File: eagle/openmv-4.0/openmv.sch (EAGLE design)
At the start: 52 parts, among them U1 OV9650, U2 USD-47571, U3 ADP222, U4 STM32F407LQFP100, U5 BEAD, U6 BEAD, U7 24FC128, X1 USB-MICROB, Y2 RESONATORSMD

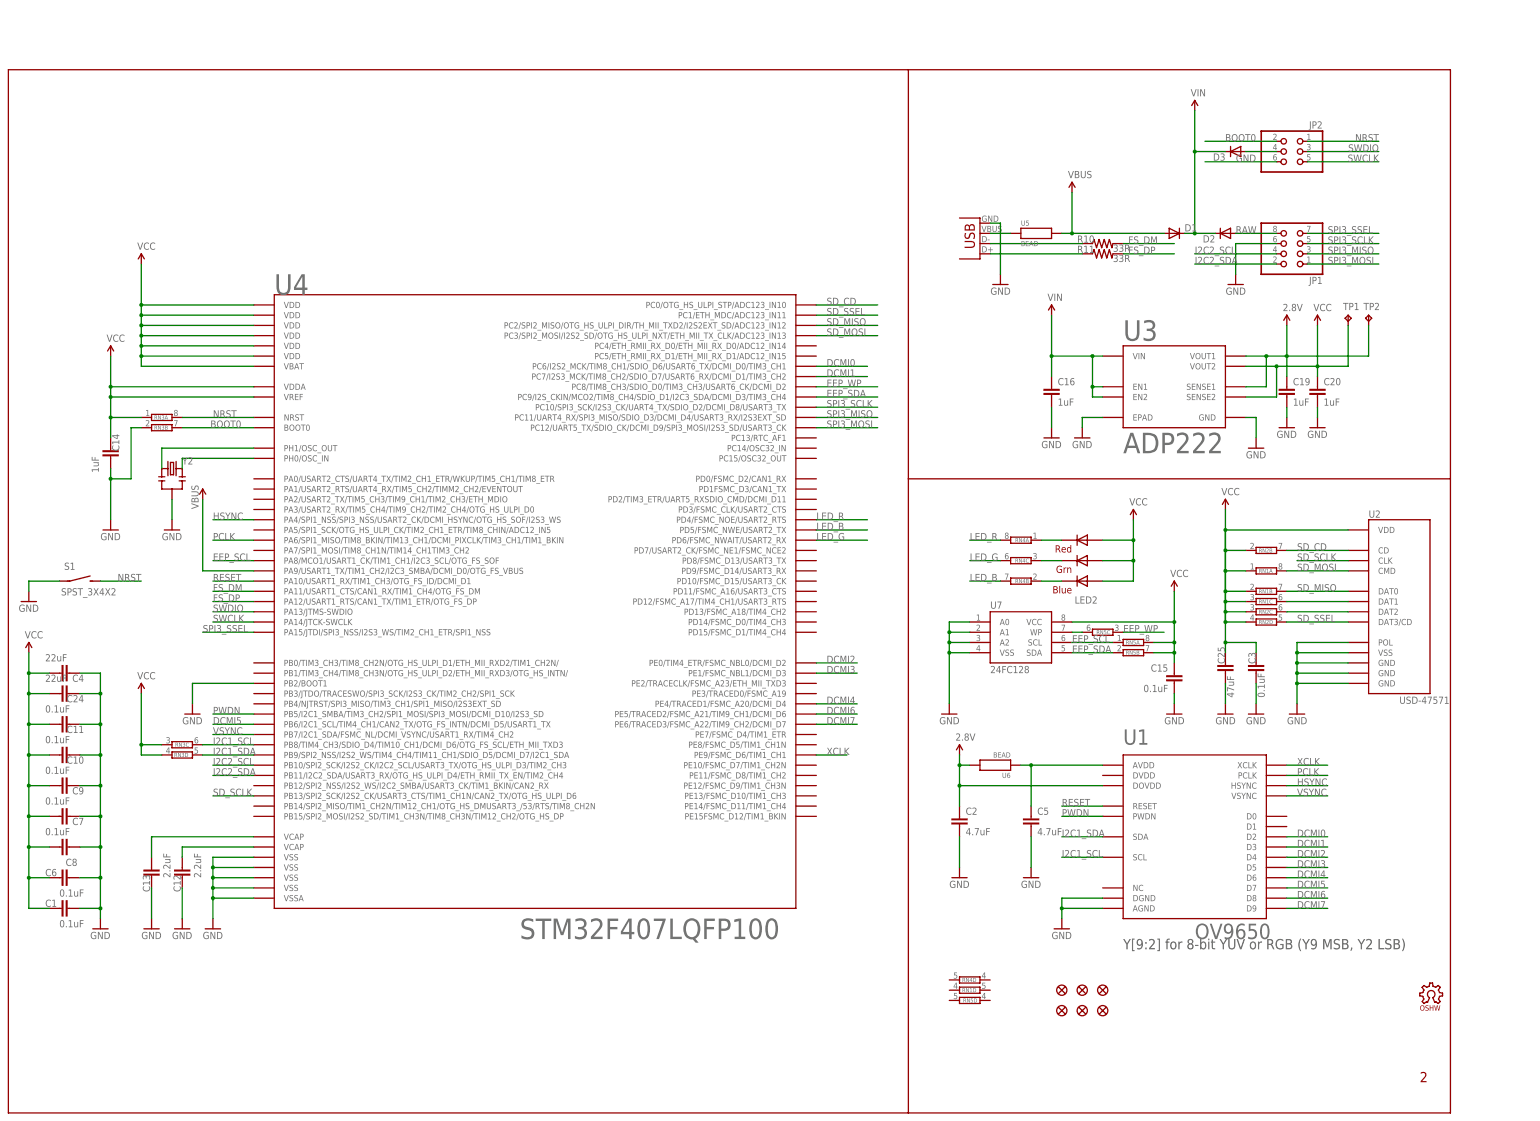
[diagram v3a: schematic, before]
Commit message: Update REV4
* Make more room for mounting holes, and dbg header
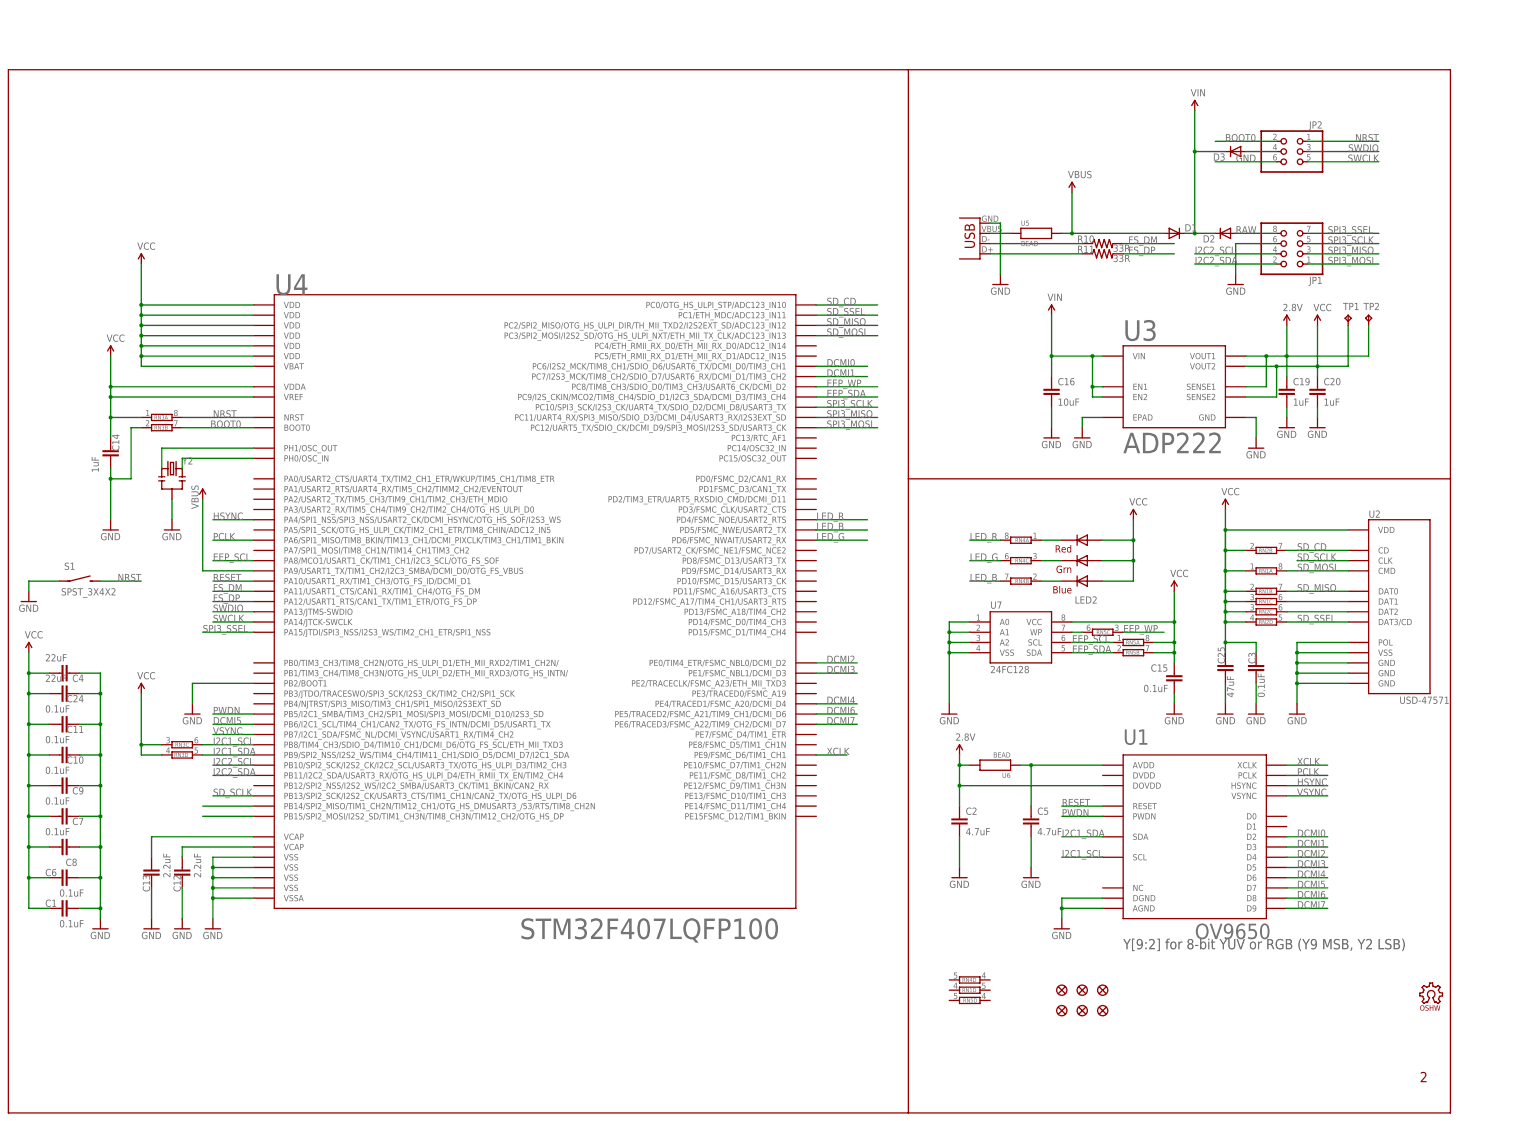
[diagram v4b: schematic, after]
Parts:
- C16: value 1uF -> 10uF; device sfe:CAP0402-CAP -> sfe:CAP0805
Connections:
- new net N$12: U4.PB14/SPI2_MISO/TIM1_CH2N/TIM12_CH1/OTG_HS_DMUSART3_/53/RTS/TIM8_CH2N
- new net N$13: U4.PB15/SPI2_MOSI/I2S2_SD/TIM1_CH3N/TIM8_CH3N/TIM12_CH2/OTG_HS_DP
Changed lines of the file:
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@@
 <part name="U$6" library="mux" deviceset="VBUS" device=""/>
 <part name="LOGO1" library="iofault" deviceset="OSHW_LOGO_FILL" device="X0150-NT"/>
-<part name="C16" library="sfe" deviceset="CAP" device="0402-CAP" value="1uF"/>
+<part name="C16" library="sfe" deviceset="CAP" device="0805" value="10uF"/>
 <part name="GND11" library="SparkFun" deviceset="GND" device=""/>
 <part name="C20" library="sfe" deviceset="CAP" device="0402-CAP" value="1uF"/>
@@
 <segment>
 <pinref part="JP2" gate="A" pin="6"/>
-<wire x1="205.74" y1="134.62" x2="187.96" y2="134.62" width="0.1524" layer="91"/>
+<wire x1="205.74" y1="134.62" x2="190.5" y2="134.62" width="0.1524" layer="91"/>
 <label x="200.66" y="134.62" size="1.778" layer="95" rot="MR0"/>
 </segment>
@@
 <segment>
 <pinref part="JP2" gate="A" pin="2"/>
-<wire x1="205.74" y1="139.7" x2="187.96" y2="139.7" width="0.1524" layer="91"/>
+<wire x1="205.74" y1="139.7" x2="190.5" y2="139.7" width="0.1524" layer="91"/>
 <label x="200.66" y="139.7" size="1.778" layer="95" rot="MR0"/>
 </segment>
@@
 </segment>
 </net>
+<net name="N$12" class="0">
+<segment>
+<pinref part="U4" gate="G$1" pin="PB14/SPI2_MISO/TIM1_CH2N/TIM12_CH1/OTG_HS_DMUSART3_/53/RTS/TIM8_CH2N"/>
+<wire x1="-48.26" y1="-25.4" x2="-60.96" y2="-25.4" width="0.1524" layer="91"/>
+</segment>
+</net>
+<net name="N$13" class="0">
+<segment>
+<pinref part="U4" gate="G$1" pin="PB15/SPI2_MOSI/I2S2_SD/TIM1_CH3N/TIM8_CH3N/TIM12_CH2/OTG_HS_DP"/>
+<wire x1="-48.26" y1="-27.94" x2="-60.96" y2="-27.94" width="0.1524" layer="91"/>
+</segment>
+</net>

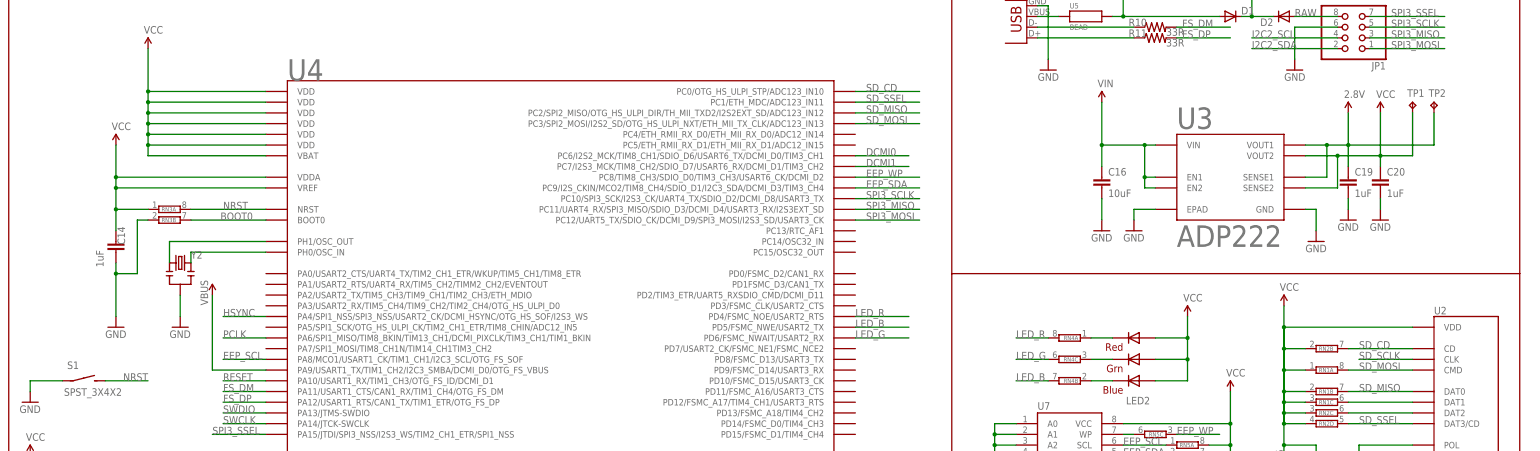
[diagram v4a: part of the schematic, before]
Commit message: Update REV4
* Replace regulator with ADP121xx
* Use the new crystal
* Fix USB connector
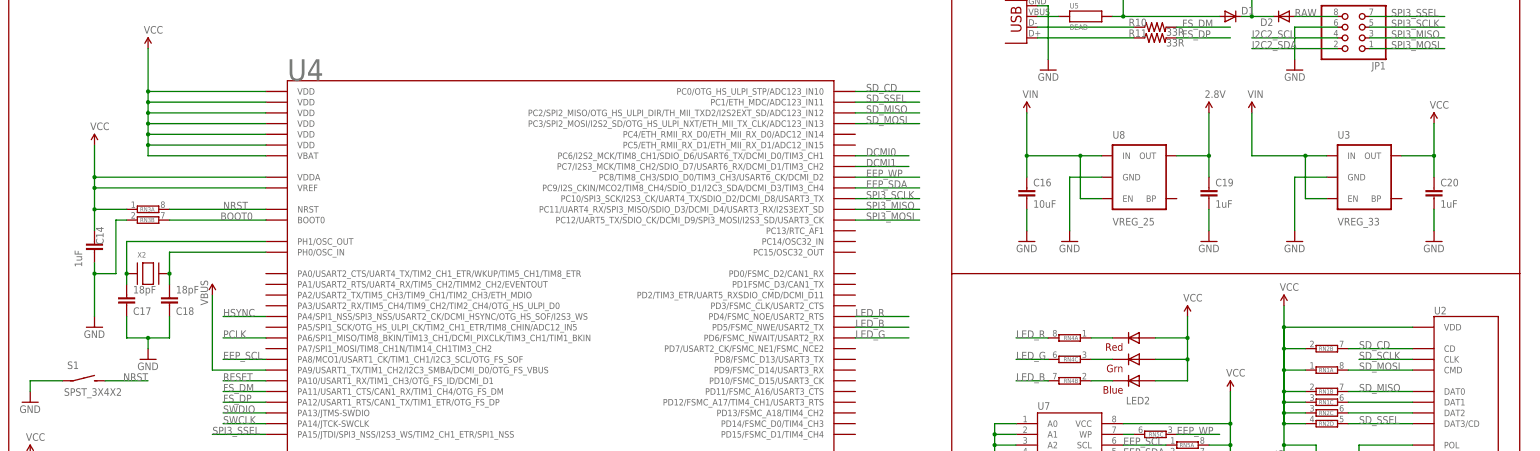
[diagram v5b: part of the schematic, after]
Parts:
- removed TP1, TP2: TPTP10R, testpad:TPTP10R
- removed Y2: RESONATORSMD, sfe:RESONATORSMD
- added C17, C18: 18pF, sfe:CAP0402-CAP
- added U8: VREG_25, sfe:V_REG_LDOSMD
- added X2: (no value), adafruit:XTALNX5032
- U3: value ADP222 -> VREG_33; device mux:ADP222 -> sfe:V_REG_LDOSMD
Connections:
- net 2.8V: now also U8.OUT; no longer TP2.TP, U3.SENSE1, U3.VOUT1
- net GND: now also C17.1, C18.1, U8.GND; no longer U3.EPAD, Y2.2
- net N$6: now also C17.2, X2.P$1; no longer Y2.1
- net N$8: now also C18.2, X2.P$2; no longer Y2.3
- net VCC: now also U3.OUT; no longer TP1.TP, U3.SENSE2, U3.VOUT2
- net VIN: now also U3.EN, U3.IN, U8.EN, U8.IN; no longer U3.EN1, U3.EN2, U3.VIN
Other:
- moved on the sheet: C14, C16, C19, C20, RN3A, RN3B
